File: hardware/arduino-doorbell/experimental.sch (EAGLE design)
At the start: 11 parts, among them T1 BC337

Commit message: Eagle Schematic update
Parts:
- R1: value 100 -> 220
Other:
- note added: "Ta"
- note added: "Tb"
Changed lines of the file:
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@@
 <parts>
 <part name="FRAME1" library="frames" deviceset="FRAME_A_L" device=""/>
-<part name="R1" library="rcl" deviceset="R-EU_" device="0204/7" value="100"/>
+<part name="R1" library="rcl" deviceset="R-EU_" device="0204/7" value="220"/>
 <part name="D1" library="diode" deviceset="1N4004" device=""/>
 <part name="X1" library="con-phoenix-254" deviceset="MPT2" device=""/>
@@
 <sheet>
 <plain>
+<text x="5.08" y="167.64" size="1.778" layer="91">Ta</text>
+<text x="5.08" y="160.02" size="1.778" layer="91">Tb</text>
 </plain>
 <instances>

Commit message: Eagle files update
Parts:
- R2: value 33k -> 10k
- R3: value 2k2 -> 1k1
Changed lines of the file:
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@@
 <part name="SUPPLY1" library="supply2" deviceset="+5V" device=""/>
 <part name="DC1" library="dc-dc-converter" deviceset="NME" device=""/>
-<part name="R2" library="rcl" deviceset="R-EU_" device="0204/7" value="33k"/>
-<part name="R3" library="rcl" deviceset="R-EU_" device="0204/7" value="2k2"/>
+<part name="R2" library="rcl" deviceset="R-EU_" device="0204/7" value="10k"/>
+<part name="R3" library="rcl" deviceset="R-EU_" device="0204/7" value="1k1"/>
 <part name="GND2" library="supply1" deviceset="GND" device=""/>
 <part name="T1" library="transistor" deviceset="BC337" device=""/>

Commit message: Eagle Schematic update
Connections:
- net A0 renamed A1
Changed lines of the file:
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@@
 </segment>
 </net>
-<net name="A0" class="0">
+<net name="A1" class="0">
 <segment>
 <pinref part="R3" gate="G$1" pin="2"/>

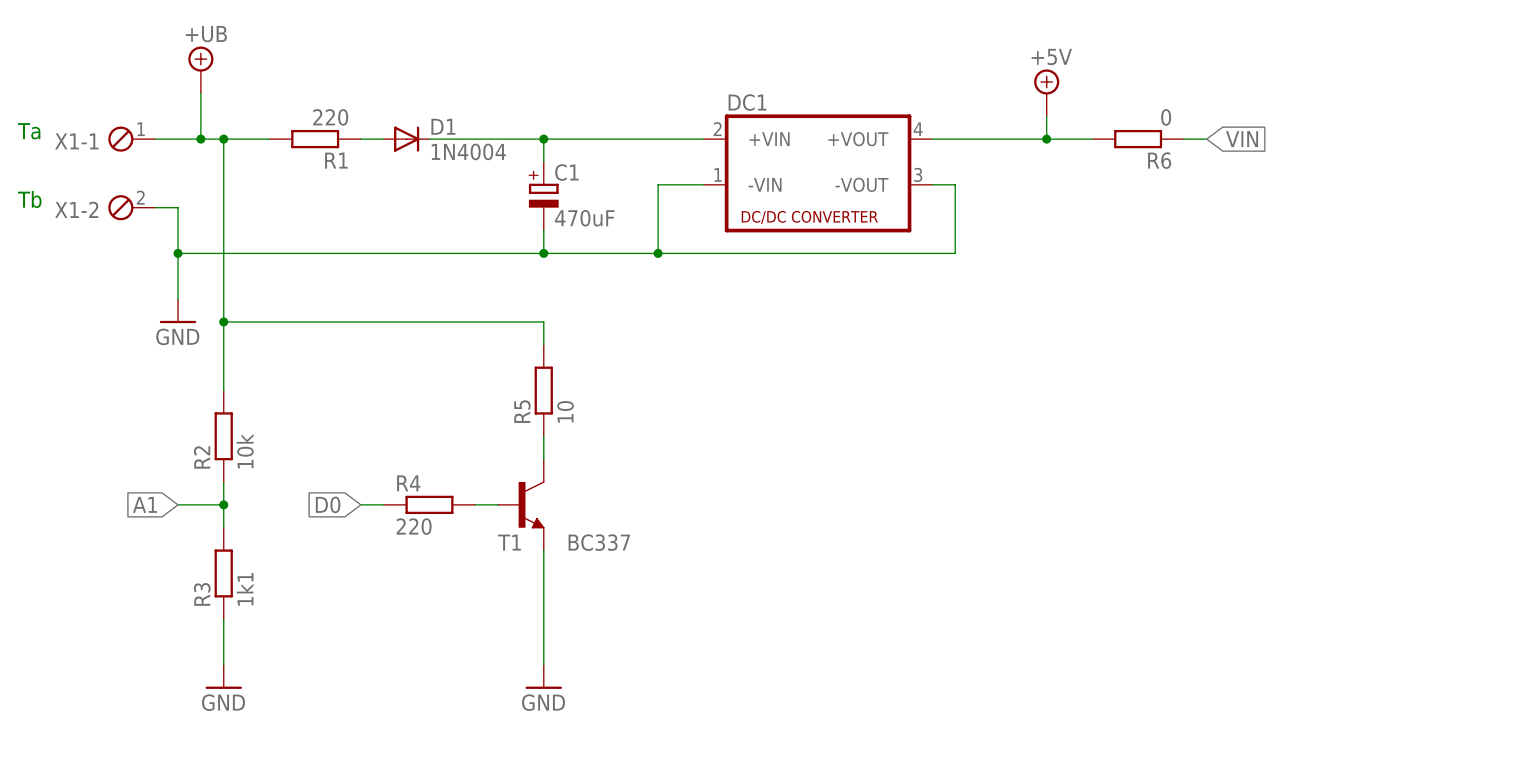
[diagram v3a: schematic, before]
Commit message: Carrier handling circuit implemented (eagle)
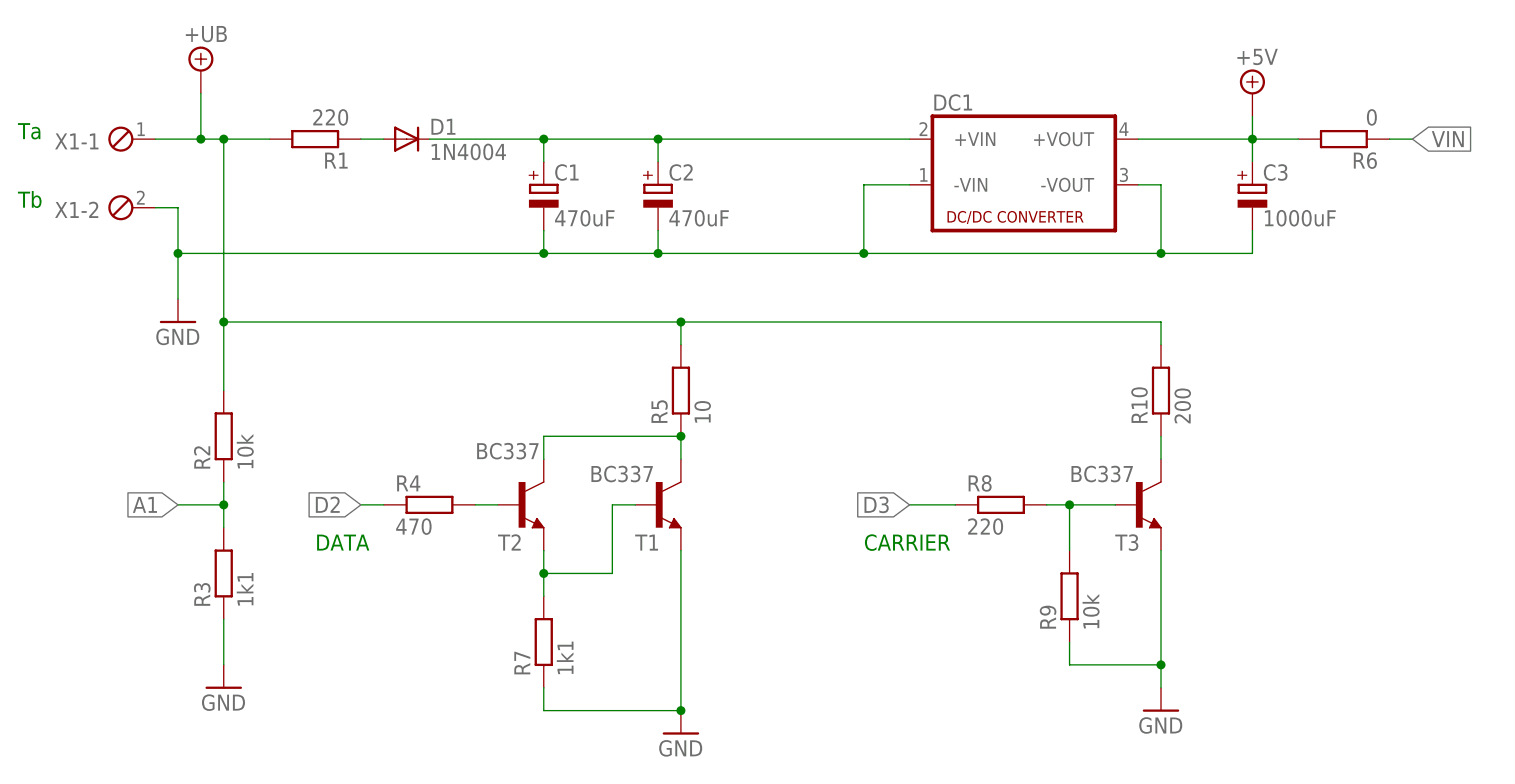
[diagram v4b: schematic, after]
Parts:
- added C2: 470uF, rcl:CPOL-EUE10-20
- added C3: 1000uF, rcl:CPOL-EUE10-20
- added R10: 200, rcl:R-EU_0204/7
- added R7: 1k1, rcl:R-EU_0204/7
- added R8: 220, rcl:R-EU_0204/7
- added R9: 10k, rcl:R-EU_0204/7
- added T2, T3: BC337, transistor:BC337
- R4: value 220 -> 470
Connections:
- net D0 renamed D2
- new net D3: R8.1
- new net N$5: R7.2, T1.B, T2.E
- new net N$6: R8.2, R9.2, T3.B
- new net N$7: R10.1, T3.C
- net +5V: now also C3.+
- net +UB: now also R10.2
- net GND: now also C2.-, C3.-, R7.1, R9.1, T3.E
- net N$1: now also C2.+
- net N$3: now also T2.B; no longer T1.B
- net N$4: now also T2.C
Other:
- note added: "CARRIER"
- note added: "DATA"
- moved on the sheet: DC1, R5, R6, T1

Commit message: Streamline schematic values
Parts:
- removed C2: 470uF, rcl:CPOL-EUE10-20
- R10: value 200 -> 220
- R4: value 470 -> 220
- R5: value 10 -> 12
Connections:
- net GND: no longer C2.-
- net N$1: no longer C2.+
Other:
- moved on the sheet: C3, DC1, R6, R7, R9
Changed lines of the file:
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@@
 <part name="GND2" library="supply1" deviceset="GND" device=""/>
 <part name="T1" library="transistor" deviceset="BC337" device=""/>
-<part name="R4" library="rcl" deviceset="R-EU_" device="0204/7" value="470"/>
-<part name="R5" library="rcl" deviceset="R-EU_" device="0204/7" value="10"/>
+<part name="R4" library="rcl" deviceset="R-EU_" device="0204/7" value="220"/>
+<part name="R5" library="rcl" deviceset="R-EU_" device="0204/7" value="12"/>
 <part name="GND3" library="supply1" deviceset="GND" device=""/>
 <part name="R6" library="rcl" deviceset="R-EU_" device="0204/7" value="0"/>
 <part name="T2" library="transistor" deviceset="BC337" device=""/>
 <part name="R7" library="rcl" deviceset="R-EU_" device="0204/7" value="1k1"/>
-<part name="C2" library="rcl" deviceset="CPOL-EU" device="E10-20" value="470uF"/>
 <part name="T3" library="transistor" deviceset="BC337" device=""/>
 <part name="R8" library="rcl" deviceset="R-EU_" device="0204/7" value="220"/>
 <part name="GND4" library="supply1" deviceset="GND" device=""/>
 <part name="R9" library="rcl" deviceset="R-EU_" device="0204/7" value="10k"/>
-<part name="R10" library="rcl" deviceset="R-EU_" device="0204/7" value="200"/>
+<part name="R10" library="rcl" deviceset="R-EU_" device="0204/7" value="220"/>
 <part name="C3" library="rcl" deviceset="CPOL-EU" device="E10-20" value="1000uF"/>
 </parts>
@@
 <instance part="C1" gate="G$1" x="63.5" y="162.56"/>
 <instance part="SUPPLY2" gate="G$1" x="25.4" y="175.26"/>
-<instance part="SUPPLY1" gate="+5V" x="142.24" y="172.72"/>
-<instance part="DC1" gate="G$1" x="116.84" y="165.1"/>
+<instance part="SUPPLY1" gate="+5V" x="119.38" y="172.72"/>
+<instance part="DC1" gate="G$1" x="93.98" y="165.1"/>
 <instance part="R2" gate="G$1" x="27.94" y="134.62" rot="R90"/>
 <instance part="R3" gate="G$1" x="27.94" y="119.38" rot="R90"/>
@@
 <instance part="R4" gate="G$1" x="50.8" y="127"/>
 <instance part="R5" gate="G$1" x="78.74" y="139.7" rot="R90"/>
-<instance part="GND3" gate="1" x="78.74" y="101.6"/>
-<instance part="R6" gate="G$1" x="152.4" y="167.64" rot="R180"/>
+<instance part="GND3" gate="1" x="78.74" y="106.68"/>
+<instance part="R6" gate="G$1" x="129.54" y="167.64" rot="R180"/>
 <instance part="T2" gate="G$1" x="60.96" y="127" smashed="yes">
 <attribute name="NAME" x="58.42" y="121.92" size="1.778" layer="95"/>
 <attribute name="VALUE" x="55.88" y="132.08" size="1.778" layer="96"/>
 </instance>
-<instance part="R7" gate="G$1" x="63.5" y="111.76" rot="R90"/>
-<instance part="C2" gate="G$1" x="76.2" y="162.56"/>
+<instance part="R7" gate="G$1" x="68.58" y="114.3" rot="R180"/>
 <instance part="T3" gate="G$1" x="129.54" y="127" smashed="yes">
 <attribute name="NAME" x="127" y="121.92" size="1.778" layer="95"/>
@@
 </instance>
 <instance part="R8" gate="G$1" x="114.3" y="127"/>
-<instance part="GND4" gate="1" x="132.08" y="104.14"/>
-<instance part="R9" gate="G$1" x="121.92" y="116.84" rot="R90"/>
+<instance part="GND4" gate="1" x="132.08" y="106.68"/>
+<instance part="R9" gate="G$1" x="121.92" y="119.38" rot="R90"/>
 <instance part="R10" gate="G$1" x="132.08" y="139.7" rot="R90"/>
-<instance part="C3" gate="G$1" x="142.24" y="162.56"/>
+<instance part="C3" gate="G$1" x="119.38" y="162.56"/>
 </instances>
 <busses>
@@
 <pinref part="DC1" gate="G$1" pin="-VIN"/>
 <wire x1="22.86" y1="154.94" x2="22.86" y2="149.86" width="0.1524" layer="91"/>
-<wire x1="104.14" y1="162.56" x2="99.06" y2="162.56" width="0.1524" layer="91"/>
-<wire x1="99.06" y1="162.56" x2="99.06" y2="154.94" width="0.1524" layer="91"/>
-<wire x1="99.06" y1="154.94" x2="76.2" y2="154.94" width="0.1524" layer="91"/>
+<wire x1="81.28" y1="162.56" x2="76.2" y2="162.56" width="0.1524" layer="91"/>
+<wire x1="76.2" y1="162.56" x2="76.2" y2="154.94" width="0.1524" layer="91"/>
+<wire x1="76.2" y1="154.94" x2="63.5" y2="154.94" width="0.1524" layer="91"/>
 <pinref part="C1" gate="G$1" pin="-"/>
-<wire x1="76.2" y1="154.94" x2="63.5" y2="154.94" width="0.1524" layer="91"/>
 <wire x1="63.5" y1="154.94" x2="63.5" y2="157.48" width="0.1524" layer="91"/>
-<wire x1="99.06" y1="154.94" x2="132.08" y2="154.94" width="0.1524" layer="91"/>
-<junction x="99.06" y="154.94"/>
+<wire x1="76.2" y1="154.94" x2="109.22" y2="154.94" width="0.1524" layer="91"/>
+<junction x="76.2" y="154.94"/>
 <pinref part="DC1" gate="G$1" pin="-VOUT"/>
-<wire x1="132.08" y1="154.94" x2="132.08" y2="162.56" width="0.1524" layer="91"/>
-<wire x1="132.08" y1="162.56" x2="129.54" y2="162.56" width="0.1524" layer="91"/>
+<wire x1="109.22" y1="154.94" x2="109.22" y2="162.56" width="0.1524" layer="91"/>
+<wire x1="109.22" y1="162.56" x2="106.68" y2="162.56" width="0.1524" layer="91"/>
 <wire x1="63.5" y1="154.94" x2="22.86" y2="154.94" width="0.1524" layer="91"/>
 <junction x="63.5" y="154.94"/>
 <junction x="22.86" y="154.94"/>
-<pinref part="C2" gate="G$1" pin="-"/>
-<wire x1="76.2" y1="157.48" x2="76.2" y2="154.94" width="0.1524" layer="91"/>
-<junction x="76.2" y="154.94"/>
 <pinref part="C3" gate="G$1" pin="-"/>
-<wire x1="132.08" y1="154.94" x2="142.24" y2="154.94" width="0.1524" layer="91"/>
-<wire x1="142.24" y1="154.94" x2="142.24" y2="157.48" width="0.1524" layer="91"/>
-<junction x="132.08" y="154.94"/>
+<wire x1="109.22" y1="154.94" x2="119.38" y2="154.94" width="0.1524" layer="91"/>
+<wire x1="119.38" y1="154.94" x2="119.38" y2="157.48" width="0.1524" layer="91"/>
+<junction x="109.22" y="154.94"/>
 </segment>
 <segment>
@@
 </segment>
 <segment>
+<pinref part="T3" gate="G$1" pin="E"/>
+<pinref part="GND4" gate="1" pin="GND"/>
+<wire x1="132.08" y1="109.22" x2="132.08" y2="111.76" width="0.1524" layer="91"/>
+<pinref part="R9" gate="G$1" pin="1"/>
+<wire x1="132.08" y1="111.76" x2="132.08" y2="121.92" width="0.1524" layer="91"/>
+<wire x1="121.92" y1="114.3" x2="121.92" y2="111.76" width="0.1524" layer="91"/>
+<wire x1="121.92" y1="111.76" x2="132.08" y2="111.76" width="0.1524" layer="91"/>
+<junction x="132.08" y="111.76"/>
+</segment>
+<segment>
 <pinref part="GND3" gate="1" pin="GND"/>
 <pinref part="T1" gate="G$1" pin="E"/>
-<wire x1="78.74" y1="104.14" x2="78.74" y2="121.92" width="0.1524" layer="91"/>
+<wire x1="78.74" y1="109.22" x2="78.74" y2="114.3" width="0.1524" layer="91"/>
 <pinref part="R7" gate="G$1" pin="1"/>
-<wire x1="63.5" y1="106.68" x2="63.5" y2="104.14" width="0.1524" layer="91"/>
-<wire x1="63.5" y1="104.14" x2="78.74" y2="104.14" width="0.1524" layer="91"/>
-<junction x="78.74" y="104.14"/>
-</segment>
-<segment>
-<pinref part="T3" gate="G$1" pin="E"/>
-<pinref part="GND4" gate="1" pin="GND"/>
-<wire x1="132.08" y1="106.68" x2="132.08" y2="109.22" width="0.1524" layer="91"/>
-<pinref part="R9" gate="G$1" pin="1"/>
-<wire x1="132.08" y1="109.22" x2="132.08" y2="121.92" width="0.1524" layer="91"/>
-<wire x1="121.92" y1="111.76" x2="121.92" y2="109.22" width="0.1524" layer="91"/>
-<wire x1="121.92" y1="109.22" x2="132.08" y2="109.22" width="0.1524" layer="91"/>
-<junction x="132.08" y="109.22"/>
+<wire x1="78.74" y1="114.3" x2="78.74" y2="121.92" width="0.1524" layer="91"/>
+<wire x1="78.74" y1="114.3" x2="73.66" y2="114.3" width="0.1524" layer="91"/>
+<junction x="78.74" y="114.3"/>
 </segment>
 </net>
@@
 <wire x1="50.8" y1="167.64" x2="63.5" y2="167.64" width="0.1524" layer="91"/>
 <pinref part="C1" gate="G$1" pin="+"/>
-<wire x1="63.5" y1="167.64" x2="76.2" y2="167.64" width="0.1524" layer="91"/>
-<wire x1="76.2" y1="167.64" x2="104.14" y2="167.64" width="0.1524" layer="91"/>
+<wire x1="63.5" y1="167.64" x2="81.28" y2="167.64" width="0.1524" layer="91"/>
 <wire x1="63.5" y1="165.1" x2="63.5" y2="167.64" width="0.1524" layer="91"/>
 <junction x="63.5" y="167.64"/>
-<pinref part="C2" gate="G$1" pin="+"/>
-<wire x1="76.2" y1="165.1" x2="76.2" y2="167.64" width="0.1524" layer="91"/>
-<junction x="76.2" y="167.64"/>
 </segment>
 </net>
@@
 <pinref part="DC1" gate="G$1" pin="+VOUT"/>
 <pinref part="SUPPLY1" gate="+5V" pin="+5V"/>
-<wire x1="129.54" y1="167.64" x2="142.24" y2="167.64" width="0.1524" layer="91"/>
-<wire x1="142.24" y1="167.64" x2="142.24" y2="170.18" width="0.1524" layer="91"/>
-<wire x1="142.24" y1="167.64" x2="147.32" y2="167.64" width="0.1524" layer="91"/>
-<junction x="142.24" y="167.64"/>
+<wire x1="106.68" y1="167.64" x2="119.38" y2="167.64" width="0.1524" layer="91"/>
+<wire x1="119.38" y1="167.64" x2="119.38" y2="170.18" width="0.1524" layer="91"/>
+<wire x1="119.38" y1="167.64" x2="124.46" y2="167.64" width="0.1524" layer="91"/>
+<junction x="119.38" y="167.64"/>
 <pinref part="R6" gate="G$1" pin="2"/>
 <pinref part="C3" gate="G$1" pin="+"/>
-<wire x1="142.24" y1="165.1" x2="142.24" y2="167.64" width="0.1524" layer="91"/>
+<wire x1="119.38" y1="165.1" x2="119.38" y2="167.64" width="0.1524" layer="91"/>
 </segment>
 </net>
@@
 <segment>
 <pinref part="R6" gate="G$1" pin="1"/>
-<wire x1="157.48" y1="167.64" x2="160.02" y2="167.64" width="0.1524" layer="91"/>
-<label x="160.02" y="167.64" size="1.778" layer="95" xref="yes"/>
+<wire x1="134.62" y1="167.64" x2="137.16" y2="167.64" width="0.1524" layer="91"/>
+<label x="137.16" y="167.64" size="1.778" layer="95" xref="yes"/>
 </segment>
 </net>
@@
 <pinref part="T2" gate="G$1" pin="E"/>
 <pinref part="R7" gate="G$1" pin="2"/>
-<wire x1="63.5" y1="116.84" x2="63.5" y2="119.38" width="0.1524" layer="91"/>
+<wire x1="63.5" y1="114.3" x2="63.5" y2="119.38" width="0.1524" layer="91"/>
 <pinref part="T1" gate="G$1" pin="B"/>
 <wire x1="63.5" y1="119.38" x2="63.5" y2="121.92" width="0.1524" layer="91"/>
@@
 <pinref part="R9" gate="G$1" pin="2"/>
 <wire x1="121.92" y1="127" x2="127" y2="127" width="0.1524" layer="91"/>
-<wire x1="121.92" y1="121.92" x2="121.92" y2="127" width="0.1524" layer="91"/>
+<wire x1="121.92" y1="124.46" x2="121.92" y2="127" width="0.1524" layer="91"/>
 <junction x="121.92" y="127"/>
 </segment>
